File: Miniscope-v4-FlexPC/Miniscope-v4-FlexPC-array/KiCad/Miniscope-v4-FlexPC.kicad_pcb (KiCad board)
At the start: 2 copper layers, 7.2 x 10.4 mm, 6 parts, among them J1 Conn_01x20, J2 Conn_01x20, J3 Conn_01x05, J4 Conn_01x05, J5 Conn_01x14, J6 Conn_01x14

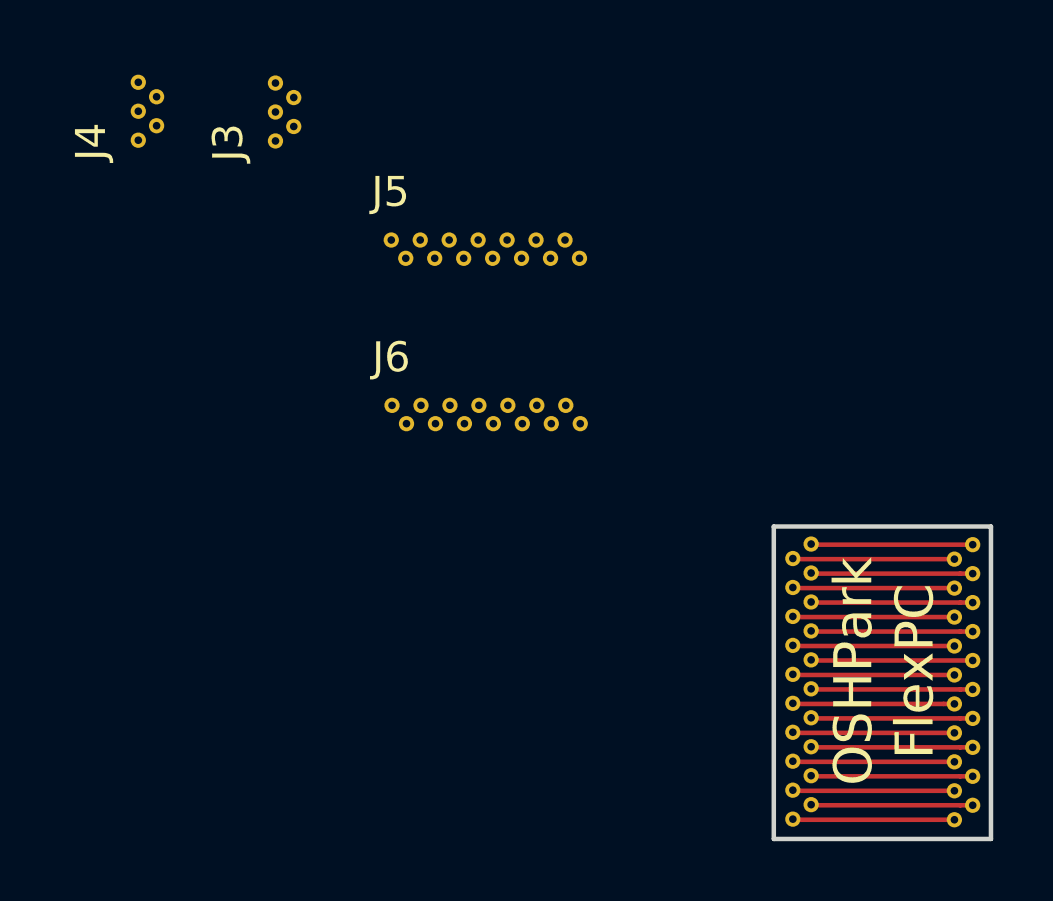
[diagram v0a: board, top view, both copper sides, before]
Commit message: Add FlexPC array for connecting all PCBs and add EWL FlexPC for connecting to EWL
This commit contains the first version of both of these FlexPCs sent to OSHPark fab on 04/25/2019.
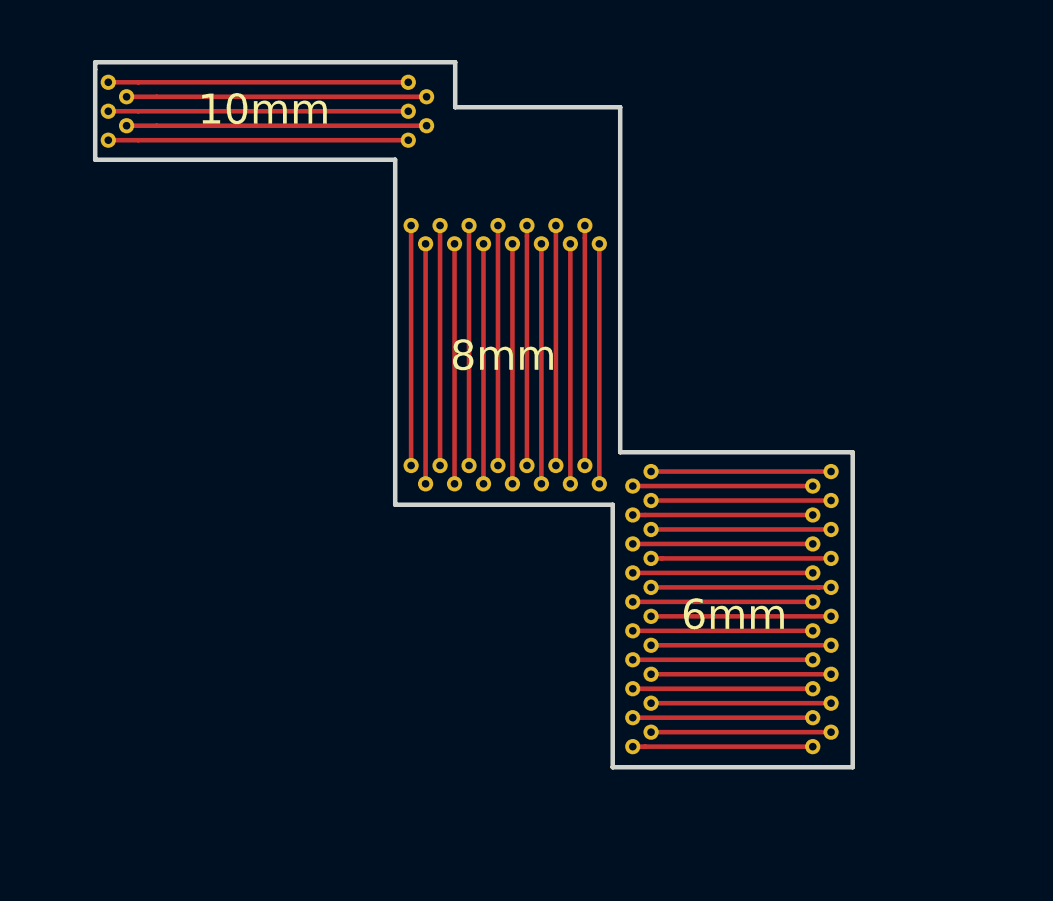
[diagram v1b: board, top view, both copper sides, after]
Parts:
- moved J2 5.86 mm to (35.3, 28.4)
- moved J1 5.31 mm to (41.3, 28.4)
- moved J3 4.43 mm to (27.2, 17.4)
- moved J6 2.10 mm to (27.3, 28.2)
- moved J4 1.00 mm to (17.2, 17.4)
- moved J5 0.82 mm to (27.3, 20.2)
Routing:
- net Net-(J3-Pad5): track 0.00 -> 10.0 mm
- net Net-(J3-Pad4): track 0.00 -> 10.0 mm
- net Net-(J3-Pad3): track 0.00 -> 10.0 mm
- net Net-(J3-Pad2): track 0.00 -> 10.0 mm
- net Net-(J3-Pad1): track 0.00 -> 10.0 mm
- net Net-(J5-Pad9): track 0.00 -> 8.00 mm
- net Net-(J5-Pad8): track 0.00 -> 8.00 mm
- net Net-(J5-Pad7): track 0.00 -> 8.00 mm
- net Net-(J5-Pad6): track 0.00 -> 8.00 mm
- net Net-(J5-Pad5): track 0.00 -> 8.00 mm
- net Net-(J5-Pad4): track 0.00 -> 8.00 mm
- net Net-(J5-Pad3): track 0.00 -> 8.00 mm
- net Net-(J5-Pad2): track 0.00 -> 8.00 mm
- net Net-(J5-Pad14): track 0.00 -> 8.00 mm
- net Net-(J5-Pad13): track 0.00 -> 8.00 mm
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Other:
- board size 7.2 x 10.4 mm -> 25.2 x 23.5 mm
- board text added: "10mm"
- board text added: "6mm"
- board text added: "8mm"
- board text removed: "OSHPark FlexPC"
